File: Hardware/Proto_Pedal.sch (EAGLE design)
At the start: 98 parts, among them J1 5.5x2.1mm Barrel, Q1 MMBT2222A, Q2 MOSFET-NCHANNEL2N7002PW, Q3 30V, 2.5A

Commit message: PCB Ready for protos
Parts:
- removed JP68: FX IN, SparkFun-Connectors:M01SMDNS
- added C2: 100uF, SparkFun-Capacitors:47UF-50V-20%(ELECT)
- added D2: RED, SparkFun-LED:LED-RED0603
- added JP86: FX OUT, SparkFun-Connectors:M031X03_NO_SILK
- added JP87: FX IN, SparkFun-Connectors:M031X03_NO_SILK
- added LOGO1: SFE_LOGO_NAME_FLAME.2_INCH, SparkFun-Aesthetics:SFE_LOGO_NAME_FLAME.2_INCH
- added LOGO3: OSHW-LOGOL, SparkFun-Aesthetics:OSHW-LOGOL
- added R4, R5: 100k, SparkFun-Resistors:100KOHM1/10W1%(0603)
- added SJ1: disable LED, SparkFun-Passives:JUMPER-PAD-2-NC_BY_PASTEFULL-BOX-SILK
- added STANDOFF1, STANDOFF2, STANDOFF3, STANDOFF4: STAND-OFF, SparkFun-Electromechanical:STAND-OFF
- JP1: value AUDIO-JACK4-.25-HORIZ-TRS -> INPUT JACK
- JP2: value AUDIO-JACK4-.25-HORIZ-TRS -> OUTPUT JACK
- JP69: value FX OUT -> (none); device SparkFun-Connectors:M01SMDNS -> SparkFun-Connectors:M031X03_NO_SILK
- S1: value (none) -> DPDT Stomp
- U1: value (none) -> TLE2426
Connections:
- new net N$25: D2.A, SJ1.2
- net FX_IN: now also JP87.1, JP87.2, JP87.3, R5.2; no longer JP68.1
- net FX_OUT: now also JP86.1, JP86.2, JP86.3, R4.2; no longer JP69.1
- net GND: now also C2.-, JP69.1, R4.1, R5.1
- net LEDA: now also SJ1.1
- net LEDK: now also D2.C
- net VCC: now also C2.+, JP69.3
- net VREF: now also JP69.2
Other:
- note added: "Clear SJ1 to disable onboard LED"
- note added: "Q1 being used as low-leakage diode. Emitter is intended to float."
- note added: "Rail-splitter IC Output is 1/2 Vcc (4.5V)"
- note added: "TP Near midpoint"
- note added: "TP Near power jack"
- moved on the sheet: C1, D1, J1, JP1, JP2, JP67, JP70, JP85, Q1, Q2, Q3, R1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

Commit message: WIP.
Redid bypass switch to 3PDT component with multiple gates.
Removed questionable LED circuit, replaced with an actual switch
section.
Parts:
- removed C1: 1.0uF, SparkFun-Capacitors:1.0UF-16V-10%(0603)
- removed D1: BAS16, SparkFun-DiscreteSemi:DIODESOD
- removed Q1: MMBT2222A, SparkFun-DiscreteSemi:TRANSISTOR_NPNMMBT2222A
- removed Q2: MOSFET-NCHANNEL2N7002PW, SparkFun-DiscreteSemi:MOSFET-NCHANNEL2N7002PW
- removed R2: 10K, SparkFun-Resistors:10KOHM1/10W1%(0603)0603
- removed S1: DPDT Stomp, SparkFun-Electromechanical:SWITCH-DPDTSTOMP-PTH
- removed U1: TLE2426, SparkFun-PowerIC:TLE2426_RAIL_SPLITTER
- added SW1: SWITCH-3PDT, SparkFun-Electromechanical:SWITCH-3PDT
- JP3, JP4, JP65, JP66, JP77, JP78: value M30NO_SILK -> (none)
- Q3: value 30V, 2.5A -> 2.5A/30V
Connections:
- removed net LEDK: D2.C, JP67.2, Q2.D
- removed net N$65: D1.A, Q1.C, Q2.G, R2.2
- removed net N$74: R2.1, S1.4
- removed net N$92: C1.1, U1.NR
- new net N$35: R1.1, SW1C.S
- net FX_IN: now also SW1A.P; no longer S1.3
- net FX_OUT: no longer S1.5
- net GND: now also D2.C, JP67.2, SW1A.O; no longer C1.2, Q1.B, Q2.S, U1.COM
- net N$70: now also SW1A.S; no longer S1.2
- net N$71: now also SW1B.P; no longer S1.1, S1.6
- net VCC: no longer D1.C, R1.1, U1.IN
- net VREF: no longer U1.OUT
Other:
- note added: "SW1 down = Active"
- note added: "SW1 up = Bypassed"
- note removed: "Incorporating reverse power protection and the Millenium 2 Bypass circuit designed by R.G. Keen, used with permission. Detailed notes on these snippets can be found at: http://www.geofex.com/article_folders/millenium/millen.htm http://www.geofex.com/Article_Folders/Millenium/The%20Next%20Millenium.pdf http://www.geofex.com/article_folders/mosswitch/mosswitch.htm"
- note removed: "Q1 being used as low-leakage diode. Emitter is intended to float."
- note removed: "Rail-splitter IC Output is 1/2 Vcc (4.5V)"
- moved on the sheet: D2, JP2, JP67, JP86, R1, R4, SJ1

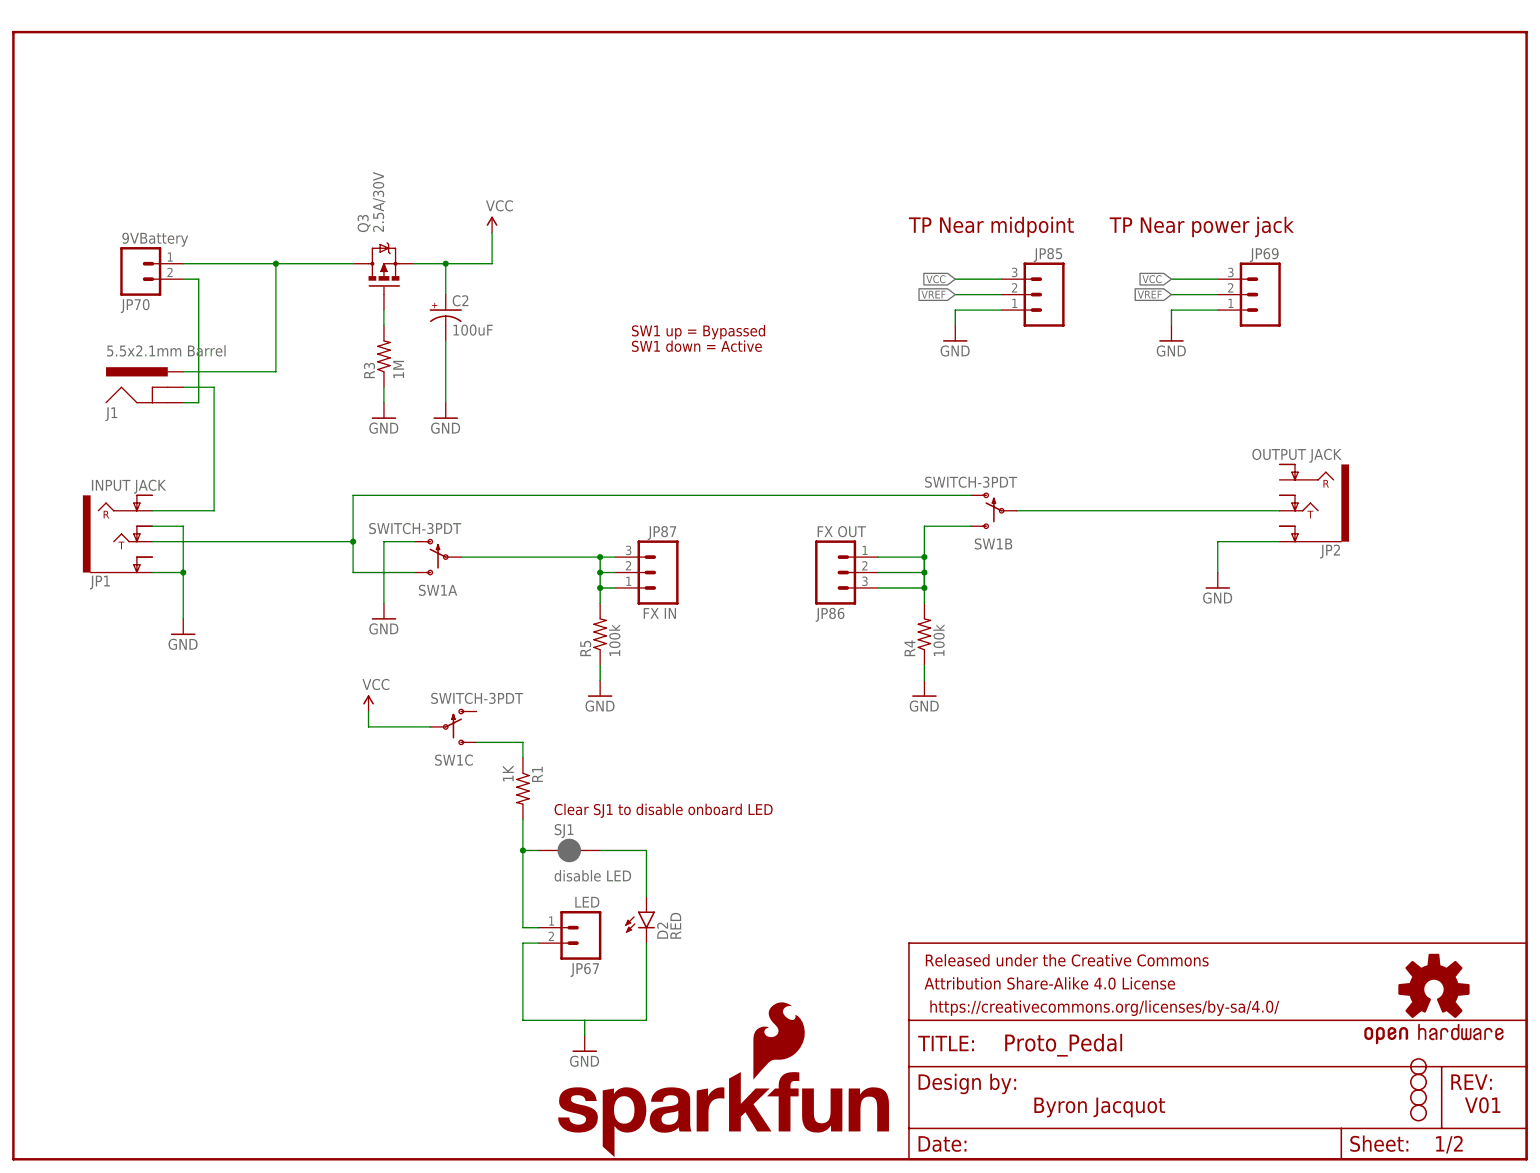
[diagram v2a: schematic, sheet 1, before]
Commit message: More WIP
Many more changes based on prototype review.
-Tip-negative power input.
-uncommited proto space for power regulation.
-Rail splitter removed
-Strain relief near 9V snap
-Some test points on i/O jacks
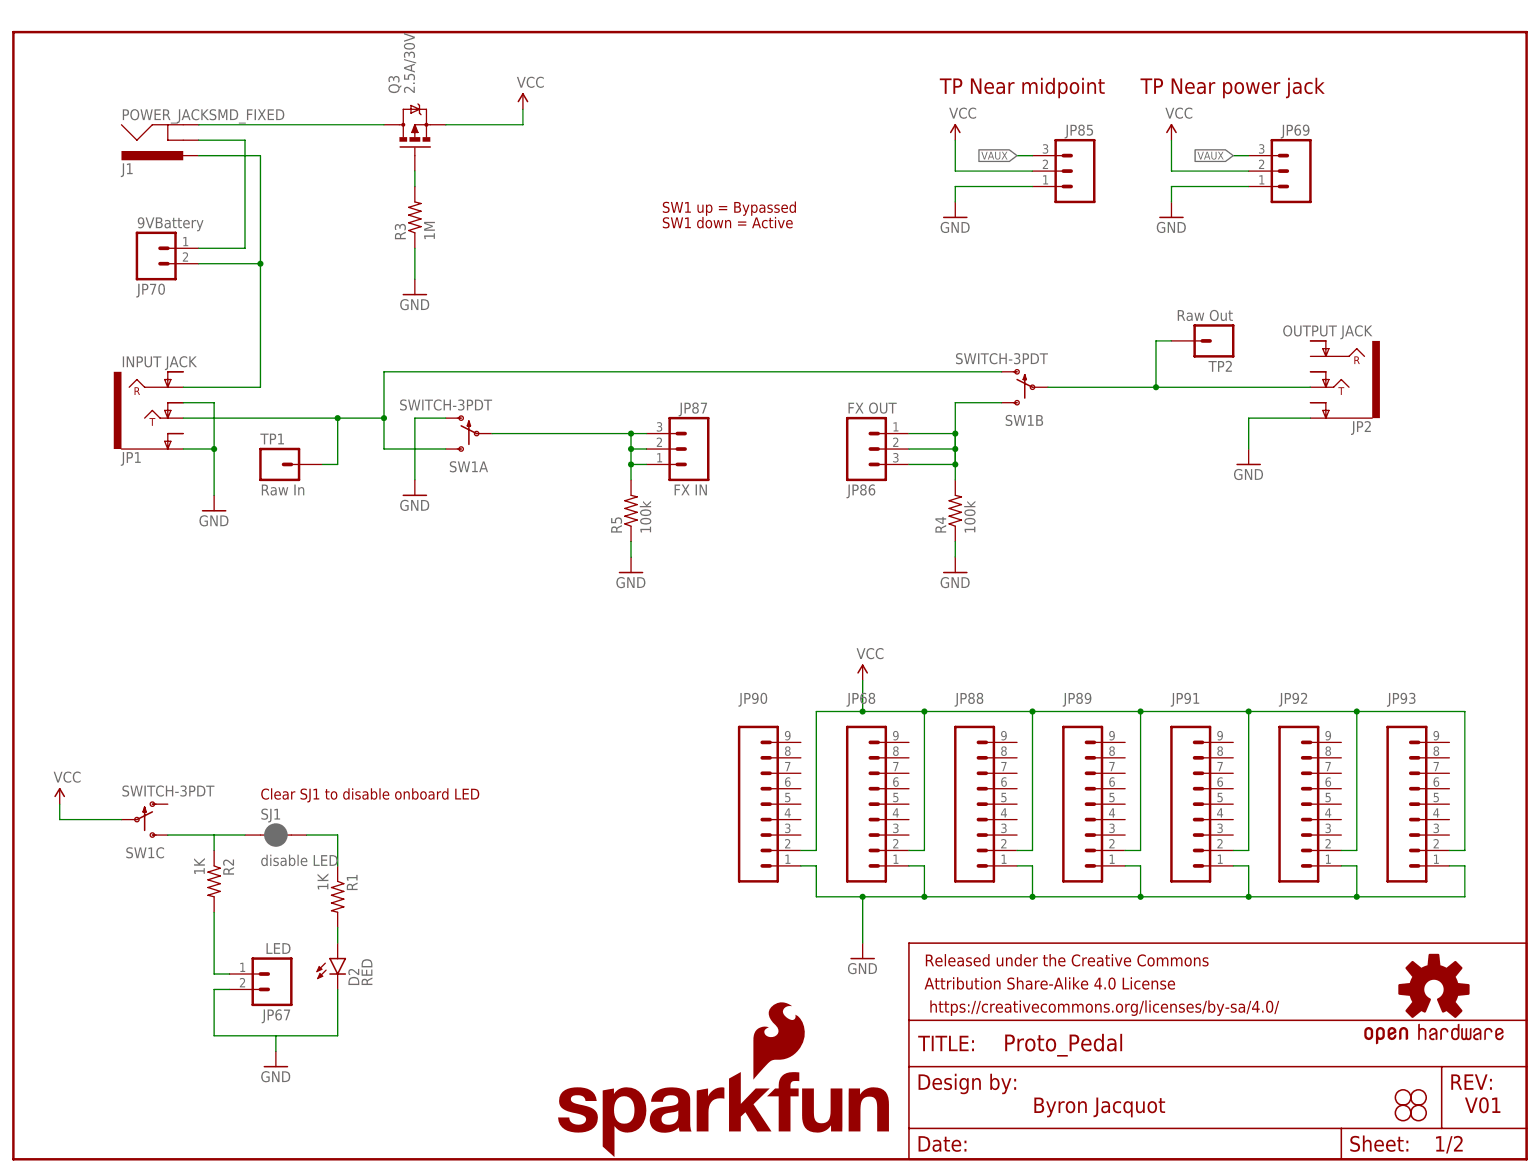
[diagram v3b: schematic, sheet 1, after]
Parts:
- removed C2: 100uF, SparkFun-Capacitors:47UF-50V-20%(ELECT)
- added JP68, JP88, JP89, JP90, JP91, JP92, JP93: (no value), SparkFun-Connectors:M09NO_SILK
- added R2: 1K, SparkFun-Resistors:1KOHM1/10W1%(0603)
- added TP1: Raw In, SparkFun-Connectors:M01PTH_NO_SILK_YES_STOP
- added TP2: Raw Out, SparkFun-Connectors:M01PTH_NO_SILK_YES_STOP
- J1: value 5.5x2.1mm Barrel -> POWER_JACKSMD_FIXED; device SparkFun-Connectors:POWER_JACKSMD -> Testing:POWER_JACKSMD_FIXED
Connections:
- removed net N$69: J1.GND, JP70.2
- removed net N$76: J1.GNDBREAK, JP1.RING
- removed net VREF: JP69.2, JP85.2
- new net N$45: J1.GNDBREAK, JP70.1
- new net N$55: J1.PWR, JP1.RING, JP70.2
- new net N$65: R1.1, SJ1.2
- new net VAUX: JP69.3, JP85.3
- net FX_OUT: now also SW1B.S
- net GND: now also JP68.1, JP88.1, JP89.1, JP90.1, JP91.1, JP92.1, JP93.1; no longer C2.-
- net LEDA: now also R2.2; no longer R1.2, SJ1.1
- net N$25: now also R1.2; no longer SJ1.2
- net N$35: now also R2.1, SJ1.1; no longer R1.1
- net N$70: now also SW1B.O, TP1.1
- net N$71: now also TP2.1
- net VBATT: now also J1.GND; no longer J1.PWR, JP70.1
- net VCC: now also JP68.2, JP69.2, JP85.2, JP88.2, JP89.2, JP90.2, JP91.2, JP92.2, JP93.2, SW1C.P; no longer C2.+, JP69.3, JP85.3
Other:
- moved on the sheet: D2, J1, JP1, JP2, JP67, JP69, JP70, JP77, JP78, JP85, JP86, JP87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

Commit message: More WIP
Much cleanup for review soon.
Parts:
- removed JP67: LED, SparkFun-Connectors:M02PTH3
- added C1: C in, Testing:DUAL_FOOTPRINT_CAP
- added C2: C out, Testing:DUAL_FOOTPRINT_CAP
- added D1: RED, SparkFun-LED:LED-RED0603
- added FID1, FID2: FIDUCIAL1X2, SparkFun-Aesthetics:FIDUCIAL1X2
- added JP94, JP95, JP96: 1x2, SparkFun-Connectors:M021X02_NO_SILK
- added TP3: Out Ring, SparkFun-Connectors:M01PTH_NO_SILK_YES_STOP
- added TP4: In Ring, SparkFun-Connectors:M01PTH_NO_SILK_YES_STOP
- added TP5: FX Input, SparkFun-Connectors:M01PTH_NO_SILK_YES_STOP
- added TP6: FX Output, SparkFun-Connectors:M01PTH_NO_SILK_YES_STOP
- D2: value RED -> PTH-LED; device SparkFun-LED:LED-RED0603 -> SparkFun-Connectors:M02PTH3
- JP10, JP11, JP12, JP13, JP14, JP15, JP16, JP17, JP18, JP19, JP20, JP21, JP22, JP23, JP24, JP25, JP26, JP27, JP28, JP29, JP30, JP31, JP32, JP33, JP34, JP35, JP36, JP37, JP38, JP39, JP40, JP41, JP42, JP43, JP44, JP45, JP46, JP47, JP48, JP49, JP5, JP50, JP51, JP52, JP53, JP54, JP56, JP57, JP58, JP59, JP6, JP60, JP61, JP62, JP63, JP64, JP7, JP8, JP9: value (none) -> 1x5
- JP3, JP4, JP65, JP66, JP77, JP78: value (none) -> 1x30
- JP55: value (none) -> v
- JP68, JP88, JP89, JP90, JP91, JP92, JP93: value (none) -> 1x9
- JP69, JP71, JP72, JP73, JP74, JP75, JP76, JP79, JP80, JP81, JP82, JP83, JP84, JP85: value (none) -> 1x3
- JP86: value FX OUT -> 1x2; device SparkFun-Connectors:M031X03_NO_SILK -> SparkFun-Connectors:M021X02_NO_SILK
- JP87: value FX IN -> 1x2; device SparkFun-Connectors:M031X03_NO_SILK -> SparkFun-Connectors:M021X02_NO_SILK
- R4, R5: value 100k -> 1M; device SparkFun-Resistors:100KOHM1/10W1%(0603) -> SparkFun-Resistors:1MOHM-1/10W-1%(0603)
- renumbered Q3 to Q1
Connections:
- new net N$66: JP2.RING, TP3.1
- new net N$67: C1.+, TP5.1
- new net N$68: C2.+, TP6.1
- net FX_IN: now also C1.-; no longer JP87.1, JP87.2, JP87.3
- net FX_OUT: now also C2.-; no longer JP86.1, JP86.2, JP86.3
- net GND: now also D1.C, D2.2, JP86.1, JP86.2, JP87.1, JP87.2, JP94.1, JP94.2, JP95.1, JP95.2, JP96.1, JP96.2; no longer D2.C, JP67.2
- net LEDA: now also D2.1; no longer JP67.1
- net N$25: now also D1.A; no longer D2.A
- net N$55: now also TP4.1
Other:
- note added: "30-row DIP proto area"
- note added: "9V Battery & Power Jack"
- note added: "As drawn: SW1 up = Bypassed SW1 down = Active"
- note added: "C1 is input coupling cap C2 is output coupling cap. Different circuits will use different values. PCB has dual footprint that accepts 2mm and 5mm radial caps."
- note added: "Clear SJ1 to disable onboard LED (D1)"
- note added: "Extra proto area intended for extra power supply conditioning or sililar functions."
- note added: "FX Goes Here"
- note added: "Input, Output and Bypass Circuitry"
- note added: "LED Active/Bypass indicator"
- note added: "Near midpoint"
- note added: "Near power jack"
- note added: "Nominal Power is 9V battery or 9V wall wart. Wall wart follows the Roland/Boss convention: *Tip is ground. *Sleeve is +9V. Q1 is wired as ideal diode, to only conduct when power is properly polarized. Reverse polarity isn't conducted, preventing damage if wrong wart is used, or if battery is mistakenly reversed. As per pedal convention, ground of power source is tied to ring of input jack. Insert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"
- note added: "Pad-per-hole area near jacks"
- note added: "Power Pins"
- note added: "TP on ground"
- note added: "V02"
- note added: "VAUX is optional auxillary voltage intended for buffered VCC/2 reference voltage."
- note removed: "Clear SJ1 to disable onboard LED"
- note removed: "SW1 down = Active"
- note removed: "SW1 up = Bypassed"
- note removed: "TP Near midpoint"
- note removed: "TP Near power jack"
- note removed: "V01"
- moved on the sheet: JP1, JP10, JP11, JP12, JP13, JP14, JP2, JP25, JP26, JP27, JP28, JP29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

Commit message: Preparing for review
Lots of little touch ups.
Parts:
- R1, R2: device SparkFun-Resistors:1KOHM1/10W1%(0603) -> SparkFun-Resistors:1KOHM-1/10W-1%(0603)
- R3: device SparkFun-Resistors:1MOHM1/10W1%(0603) -> SparkFun-Resistors:1MOHM-1/10W-1%(0603)
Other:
- moved on the sheet: J1, Q1, R3
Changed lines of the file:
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@@
 <part name="GND1" library="SparkFun-Aesthetics" deviceset="GND" device=""/>
 <part name="SUPPLY2" library="SparkFun-Aesthetics" deviceset="VCC" device=""/>
-<part name="R1" library="SparkFun-Resistors" deviceset="1KOHM1/10W1%(0603)" device="" value="1K"/>
+<part name="R1" library="SparkFun-Resistors" deviceset="1KOHM-1/10W-1%(0603)" device="" value="1K"/>
 <part name="D2" library="SparkFun-Connectors" deviceset="M02" device="PTH3" value="PTH-LED"/>
 <part name="GND2" library="SparkFun-Aesthetics" deviceset="GND" device=""/>
@@
 <part name="Q1" library="SparkFun-DiscreteSemi" deviceset="MOSFET-PCHANNEL" device="DMG2307L" value="2.5A/30V"/>
 <part name="GND4" library="SparkFun-Aesthetics" deviceset="GND" device=""/>
-<part name="R3" library="SparkFun-Resistors" deviceset="1MOHM1/10W1%(0603)" device="" value="1M"/>
+<part name="R3" library="SparkFun-Resistors" deviceset="1MOHM-1/10W-1%(0603)" device="" value="1M"/>
 <part name="JP77" library="SparkFun-Connectors" deviceset="M30" device="NO_SILK" value="1x30"/>
 <part name="JP78" library="SparkFun-Connectors" deviceset="M30" device="NO_SILK" value="1x30"/>
@@
 <part name="GND9" library="SparkFun-Aesthetics" deviceset="GND" device=""/>
 <part name="SUPPLY5" library="SparkFun-Aesthetics" deviceset="VCC" device=""/>
-<part name="R2" library="SparkFun-Resistors" deviceset="1KOHM1/10W1%(0603)" device="" value="1K"/>
+<part name="R2" library="SparkFun-Resistors" deviceset="1KOHM-1/10W-1%(0603)" device="" value="1K"/>
 <part name="SUPPLY6" library="SparkFun-Aesthetics" deviceset="VCC" device=""/>
 <part name="SUPPLY7" library="SparkFun-Aesthetics" deviceset="VCC" device=""/>
@@
 <instance part="GND3" gate="1" x="195.58" y="99.06"/>
 <instance part="JP70" gate="G$1" x="22.86" y="149.86" rot="MR180"/>
-<instance part="J1" gate="G$1" x="27.94" y="172.72" rot="MR180"/>
-<instance part="Q1" gate="G$1" x="66.04" y="170.18" rot="R90"/>
+<instance part="J1" gate="G$1" x="27.94" y="170.18" rot="MR180"/>
+<instance part="Q1" gate="G$1" x="66.04" y="167.64" rot="R90"/>
 <instance part="GND4" gate="1" x="66.04" y="142.24"/>
-<instance part="R3" gate="G$1" x="66.04" y="154.94" rot="R90"/>
+<instance part="R3" gate="G$1" x="66.04" y="152.4" rot="R90"/>
 <instance part="JP85" gate="G$1" x="71.12" y="71.12" rot="MR0"/>
 <instance part="GND6" gate="1" x="50.8" y="63.5"/>
@@
 <segment>
 <pinref part="GND4" gate="1" pin="GND"/>
-<wire x1="66.04" y1="149.86" x2="66.04" y2="144.78" width="0.1524" layer="91"/>
+<wire x1="66.04" y1="147.32" x2="66.04" y2="144.78" width="0.1524" layer="91"/>
 <pinref part="R3" gate="G$1" pin="1"/>
 </segment>
@@
 <pinref part="Q1" gate="G$1" pin="S"/>
 <pinref part="SUPPLY1" gate="G$1" pin="VCC"/>
-<wire x1="71.12" y1="170.18" x2="83.82" y2="170.18" width="0.1524" layer="91"/>
-<wire x1="83.82" y1="170.18" x2="83.82" y2="172.72" width="0.1524" layer="91"/>
+<wire x1="71.12" y1="167.64" x2="83.82" y2="167.64" width="0.1524" layer="91"/>
+<wire x1="83.82" y1="167.64" x2="83.82" y2="172.72" width="0.1524" layer="91"/>
 </segment>
 <segment>
@@
 <pinref part="Q1" gate="G$1" pin="D"/>
 <pinref part="J1" gate="G$1" pin="GND"/>
-<wire x1="30.48" y1="170.18" x2="60.96" y2="170.18" width="0.1524" layer="91"/>
+<wire x1="30.48" y1="167.64" x2="60.96" y2="167.64" width="0.1524" layer="91"/>
 </segment>
 </net>
@@
 <pinref part="R3" gate="G$1" pin="2"/>
 <pinref part="Q1" gate="G$1" pin="G"/>
-<wire x1="66.04" y1="160.02" x2="66.04" y2="162.56" width="0.1524" layer="91"/>
+<wire x1="66.04" y1="157.48" x2="66.04" y2="160.02" width="0.1524" layer="91"/>
 </segment>
 </net>
@@
 <pinref part="JP70" gate="G$1" pin="1"/>
 <wire x1="30.48" y1="149.86" x2="38.1" y2="149.86" width="0.1524" layer="91"/>
-<wire x1="38.1" y1="149.86" x2="38.1" y2="167.64" width="0.1524" layer="91"/>
+<wire x1="38.1" y1="149.86" x2="38.1" y2="165.1" width="0.1524" layer="91"/>
 <pinref part="J1" gate="G$1" pin="GNDBREAK"/>
-<wire x1="38.1" y1="167.64" x2="30.48" y2="167.64" width="0.1524" layer="91"/>
+<wire x1="38.1" y1="165.1" x2="30.48" y2="165.1" width="0.1524" layer="91"/>
 </segment>
 </net>
@@
 <wire x1="30.48" y1="147.32" x2="40.64" y2="147.32" width="0.1524" layer="91"/>
 <pinref part="J1" gate="G$1" pin="PWR"/>
-<wire x1="30.48" y1="165.1" x2="40.64" y2="165.1" width="0.1524" layer="91"/>
-<wire x1="40.64" y1="165.1" x2="40.64" y2="147.32" width="0.1524" layer="91"/>
+<wire x1="30.48" y1="162.56" x2="40.64" y2="162.56" width="0.1524" layer="91"/>
+<wire x1="40.64" y1="162.56" x2="40.64" y2="147.32" width="0.1524" layer="91"/>
 <junction x="40.64" y="147.32"/>
 <pinref part="TP4" gate="G$1" pin="1"/>
